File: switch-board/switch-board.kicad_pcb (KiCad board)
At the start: 2 copper layers, 149.9 x 43.8 mm, 61 parts, among them IC1 OPTO-TRANSISTOR4, IC2 OPTO-TRANSISTOR4, IC3 OPTO-TRANSISTOR4, IC4 OPTO-TRANSISTOR4, IC5 OPTO-TRANSISTOR4, IC6 OPTO-TRANSISTOR4, IC7 OPTO-TRANSISTOR4, IC8 OPTO-TRANSISTOR4, P1 CONN_01X04, P10 CONN_01X02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

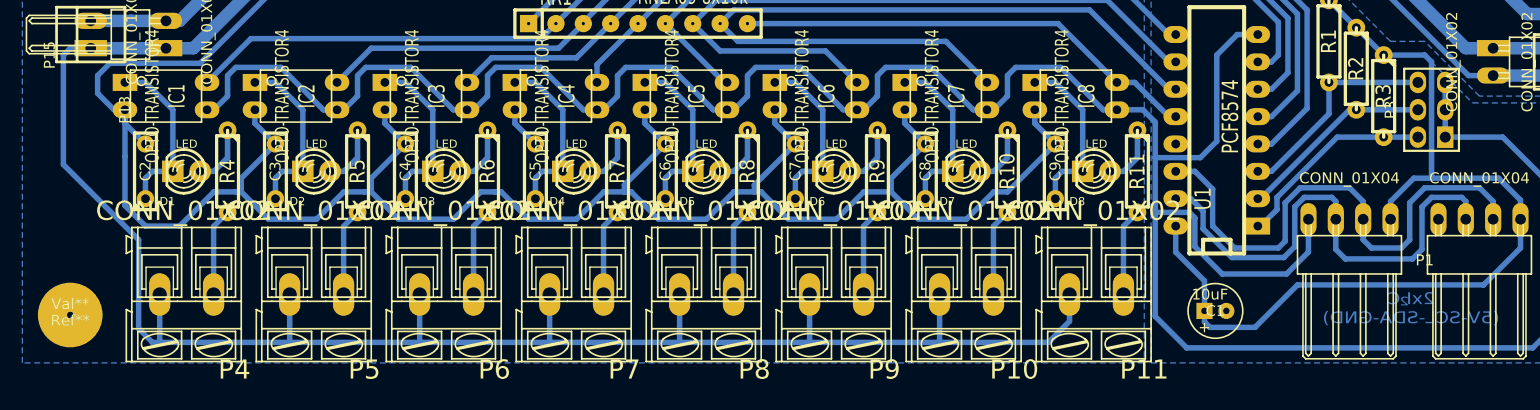
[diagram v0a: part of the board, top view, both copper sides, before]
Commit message: [switch-board] Updated PCB to look better.
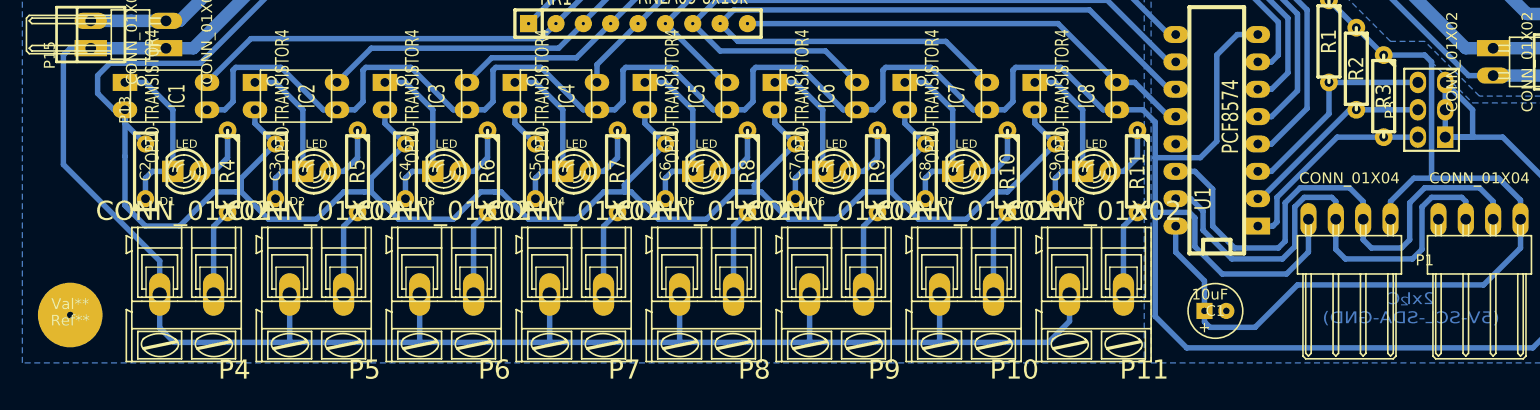
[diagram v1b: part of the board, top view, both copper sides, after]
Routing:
- net GND: track 246.4 -> 259.2 mm
- net +5VD: track 300.0 -> 294.3 mm
- net N-0000012: track 19.2 -> 19.9 mm

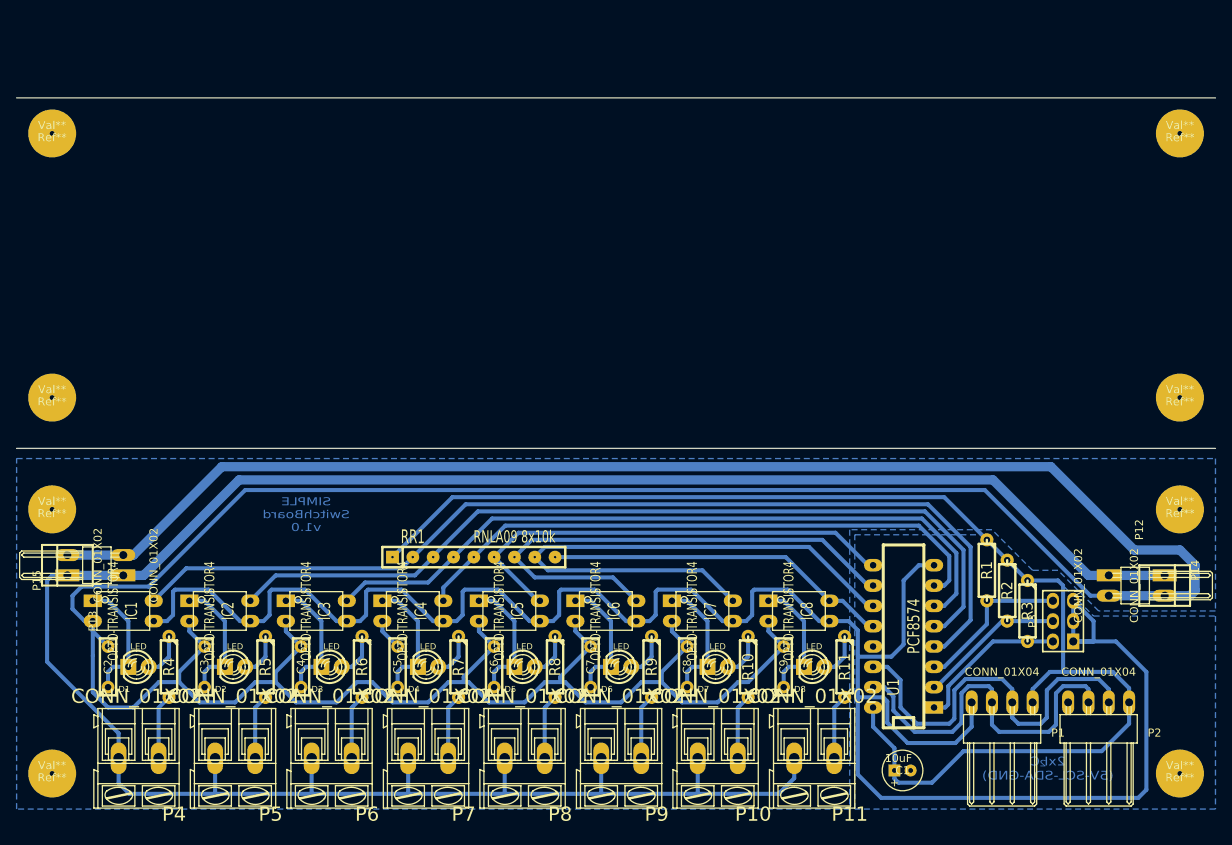
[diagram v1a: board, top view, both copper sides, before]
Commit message: [switch-board] Screw holes enlarged and rearranged.
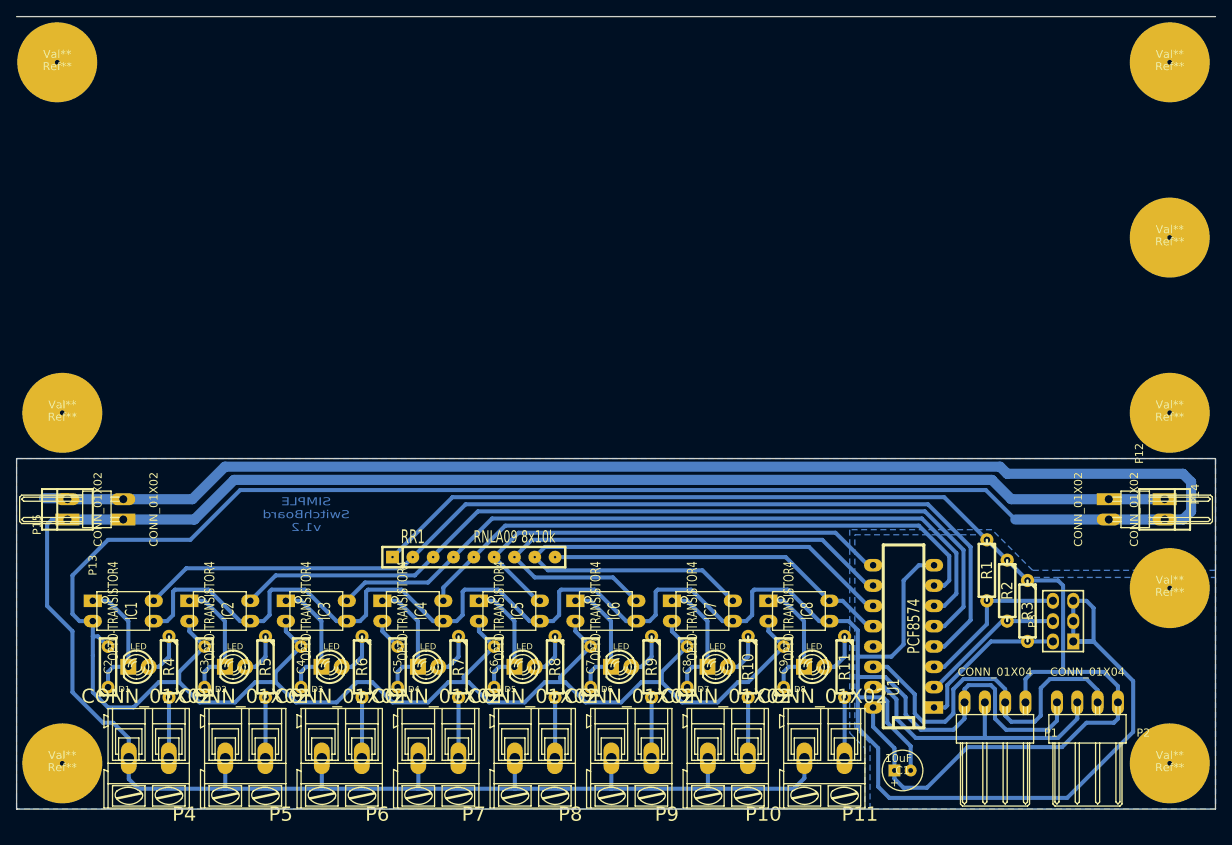
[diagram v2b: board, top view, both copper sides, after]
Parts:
- moved Ref** 143.8 mm to (229.2, 129.2)
- moved Ref** 9.92 mm to (229.2, 173.0)
- moved P12 9.53 mm to (221.6, 163.2)
- moved P14 9.53 mm to (228.6, 163.2)
- moved Ref** 8.98 mm to (229.2, 107.3)
- moved Ref** 8.91 mm to (90.2, 107.3)
- moved P13 6.99 mm to (98.4, 163.2)
- moved P15 6.99 mm to (91.4, 163.2)
- moved Ref** 2.29 mm to (90.8, 151.1)
- moved Ref** 2.29 mm to (229.2, 151.1)
- moved Ref** 1.80 mm to (90.8, 194.9)
- moved Ref** 1.80 mm to (229.2, 194.9)
- moved P2 1.40 mm to (218.9, 187.3)
- moved P10 1.27 mm to (174.0, 194.3)
- moved P11 1.27 mm to (186.1, 194.3)
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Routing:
- net GND: track 259.2 -> 283.7 mm
- net N-0000029: track 46.5 -> 37.3 mm
- net DGND: track 483.8 -> 475.4 mm
- net N-0000030: track 50.3 -> 46.8 mm
- net +5VD: track 294.3 -> 290.9 mm
- net +5V: track 164.8 -> 163.9 mm
- net N-000009: track 8.16 -> 7.63 mm
- net N-000002: track 8.16 -> 7.63 mm
- net N-0000013: track 8.16 -> 7.63 mm
- net N-000005: track 8.16 -> 7.63 mm
- net N-000007: track 8.16 -> 7.63 mm
- net N-000006: track 8.16 -> 7.63 mm
- net N-000004: track 8.16 -> 7.63 mm
- net N-000003: track 8.16 -> 7.63 mm
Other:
- board size 149.9 x 43.8 mm -> 149.9 x 99.1 mm
- board text added: "SIMPLE SwitchBoard v1.2"
- board text removed: "2"
- board text removed: "2xI C (5V-SCL-SDA-GND)"
- board text removed: "SIMPLE SwitchBoard v1.0"
